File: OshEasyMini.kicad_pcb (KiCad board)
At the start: 6 copper layers, 20 x 37.4 mm, 119 parts, among them J1 TAGCONNECT, J10 Conn_01x04_MountingPin, J11 Conn_01x02, J3 SMA_Edgelaunch, J5 UFL, J6 Conn_01x05, J7 Conn_01x06, J8 Conn_01x02, Q1 SiA449DJ, Q2 AO3400A, Q3 SiA449DJ, U11 CPT-7502-65-SMT-TR, U12 LM293QT, U17 MCP73831-2-OT, U18 TC2185-3.3VxCTTR, U19 W25Q64JVXGIQ, U2 WE-TVS-82400102, U20 SISB46DN, U21 SN74LVC1G80QDCKTQ1, U3 ADXL375, U4 MS5607-02BA, U5 MAX-M10S, U6 MCP130-xxxxTT, U7 DRV5012AEDMRR, U8 CC1200, U9 ATSAMD21G17D-A, X2 ECS-160-8-36Q-AES-TR1, Y1 ABM8W-40.0000MHZ

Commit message: good progress, changed to mia-m10
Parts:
- removed C11, C12, C14, C15, C28: 47nF, Capacitor_SMD:C_0402_1005Metric
- removed J11: Conn_01x02, Connector_PinHeader_2.54mm:PinHeader_1x02_P2.54mm_Vertical_SMD_Pin1Left
- removed J6: Conn_01x05, Connector_PinHeader_2.54mm:PinHeader_1x05_P2.54mm_Vertical
- removed J7: Conn_01x06, Connector_PinHeader_2.54mm:PinHeader_1x06_P2.54mm_Vertical
- removed J8: Conn_01x02, Connector_PinHeader_2.54mm:PinHeader_1x02_P2.54mm_Vertical
- removed R38, R39: 1k, Resistor_SMD:R_0402_1005Metric
- removed U5: MAX-M10S, RF_GPS:ublox_MAX
- added C47: 47nF, Capacitor_SMD:C_0201_0603Metric, B.Cu at (95.7, 43.4)
- added C48: 47nF, Capacitor_SMD:C_0201_0603Metric, B.Cu at (94.7, 35.7)
- added C49: 47nF, Capacitor_SMD:C_0201_0603Metric, B.Cu at (99.8, 41.2)
- added C50: 47nF, Capacitor_SMD:C_0201_0603Metric, B.Cu at (95.0, 43.4)
- added C51: 47nF, Capacitor_SMD:C_0201_0603Metric, B.Cu at (97.2, 43.4)
- added C52: 47pF, Capacitor_SMD:C_0402_1005Metric, B.Cu at (97.0, 55.1)
- added FL1: SAFFB1G58KA0F0A, Filter:Filter_1109-5_1.1x0.9mm, B.Cu at (95.9, 55.3)
- added J2: Screw_Terminal_01x03, FCU2025Lib:Horizontal2.5mmWago3pin, F.Cu at (94.1, 55.0)
- added J4: Conn_01x02, Connector_JST:JST_PH_B2B-PH-K_1x02_P2.00mm_Vertical, F.Cu at (100.6, 62.1)
- added R55: 100k, Resistor_SMD:R_0201_0603Metric, F.Cu at (94.5, 58.6)
- added R57: 0, Resistor_SMD:R_0201_0603Metric, B.Cu at (97.5, 47.4)
- added R58: 0, Resistor_SMD:R_0201_0603Metric, B.Cu at (97.6, 46.8)
- added R59: 1k, Resistor_SMD:R_0201_0603Metric, F.Cu at (94.5, 60.3)
- added U1: MIA-M10Q, Package_LGA:ublox_LGA-53_4.5x4.5mm_Layout9x9_P0.5mm, B.Cu at (93.3, 51.4)
- added Y2: 32.768khz, Crystal:Crystal_SMD_2012-2Pin_2.0x1.2mm, B.Cu at (93.2, 55.7)
- C29, C30, C32, C34: footprint Capacitor_SMD:C_0402_1005Metric -> Capacitor_SMD:C_0201_0603Metric
- R11, R50, R51, R53, R56: footprint Resistor_SMD:R_0402_1005Metric -> Resistor_SMD:R_0201_0603Metric
- R52: value 100k -> 1k; footprint Resistor_SMD:R_0402_1005Metric -> Resistor_SMD:R_0201_0603Metric
- Y1: value ABM8W-40.0000MHZ -> 40mhz 8pF 30 Ohms; footprint Crystal:Crystal_SMD_Abracon_ABM8G-4Pin_3.2x2.5mm -> Crystal:Crystal_SMD_Abracon_ABM10-4Pin_2.5x2.0mm
- moved R9 79.9 mm to (130.4, 51.7), turned to -90 degrees
- moved R10 79.6 mm to (130.4, 49.8), turned to 90 degrees
- moved U2 74.6 mm to (127.8, 50.9), turned to 180 degrees
- moved C19 27.7 mm to (100.8, 46.5), turned to 0 degrees
- moved C16 26.8 mm to (104.0, 41.1), turned to -90 degrees
- moved C45 25.7 mm to (104.0, 39.3), turned to -90 degrees
- moved J10 24.9 mm to (134.2, 50.3)
- moved C5 20.2 mm to (92.0, 45.8), turned to 0 degrees
- moved U9 19.8 mm to (98.4, 40.8), turned to -90 degrees
- moved D3 17.7 mm to (126.4, 58.4)
- moved R4 17.7 mm to (125.9, 56.0)
- moved R3 17.7 mm to (126.9, 56.1)
- moved X2 17.0 mm to (91.7, 43.5), turned to -90 degrees
- moved U19 14.3 mm to (100.4, 50.4), turned to 90 degrees
- moved C6 14.2 mm to (91.7, 41.3), turned to 180 degrees
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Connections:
- C32 pad 2: Net-(U8-DCPL_PFD_CHP) -> +3V3
- C34 pad 2: Net-(U8-DCPL_XOSC) -> +3V3
- R51 pad 1: Net-(D5-A1) -> Net-(U21-D)
- R51 pad 2: Net-(U21-D) -> Net-(D5-A1)
- R52 pad 1: GND -> Net-(D4-K1)
- R52 pad 2: Net-(JP1-A) -> GND
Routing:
- net VBUS: track 2.33 -> 9.09 mm
- net /NRST: track 0.35 -> 5.91 mm, vias 0 -> 1
- net Net-(J10-Pin_1): track 0.00 -> 4.71 mm
- net Net-(J5-In): track 6.87 -> 3.14 mm
- net Net-(D6-A): track 0.00 -> 3.33 mm
- net Net-(U8-LPF0): track 0.00 -> 3.13 mm
- net Net-(U1-RF_IN): track 0.00 -> 2.77 mm
- net Net-(U1-RTC_O): track 0.00 -> 2.58 mm
- net Net-(U1-RTC_I): track 0.00 -> 2.48 mm
- net Net-(U8-DCPL_PFD_CHP): track 3.91 -> 1.72 mm
- net Net-(J10-Pin_2): track 0.00 -> 1.99 mm
- net Net-(U8-DCPL_XOSC): track 3.37 -> 1.56 mm
- net GND: track 16.4 -> 18.2 mm, vias 10 -> 4
- net Net-(U1-VCC_RF): track 1.90 -> 3.55 mm, vias 0 -> 2
- net +3V3: track 38.3 -> 39.9 mm, vias 8 -> 4
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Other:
- board size 20 x 37.4 mm -> 17.2 x 35.4 mm

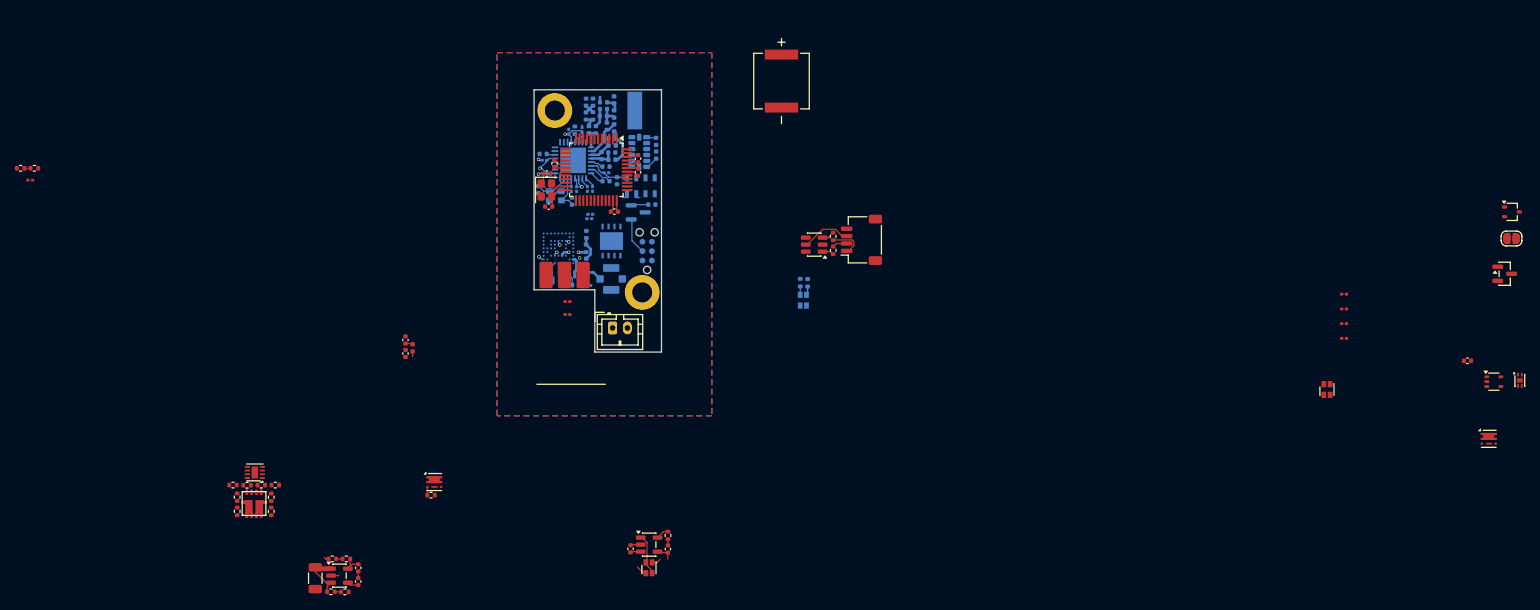
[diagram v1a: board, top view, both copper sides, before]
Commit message: all components placed currently routing
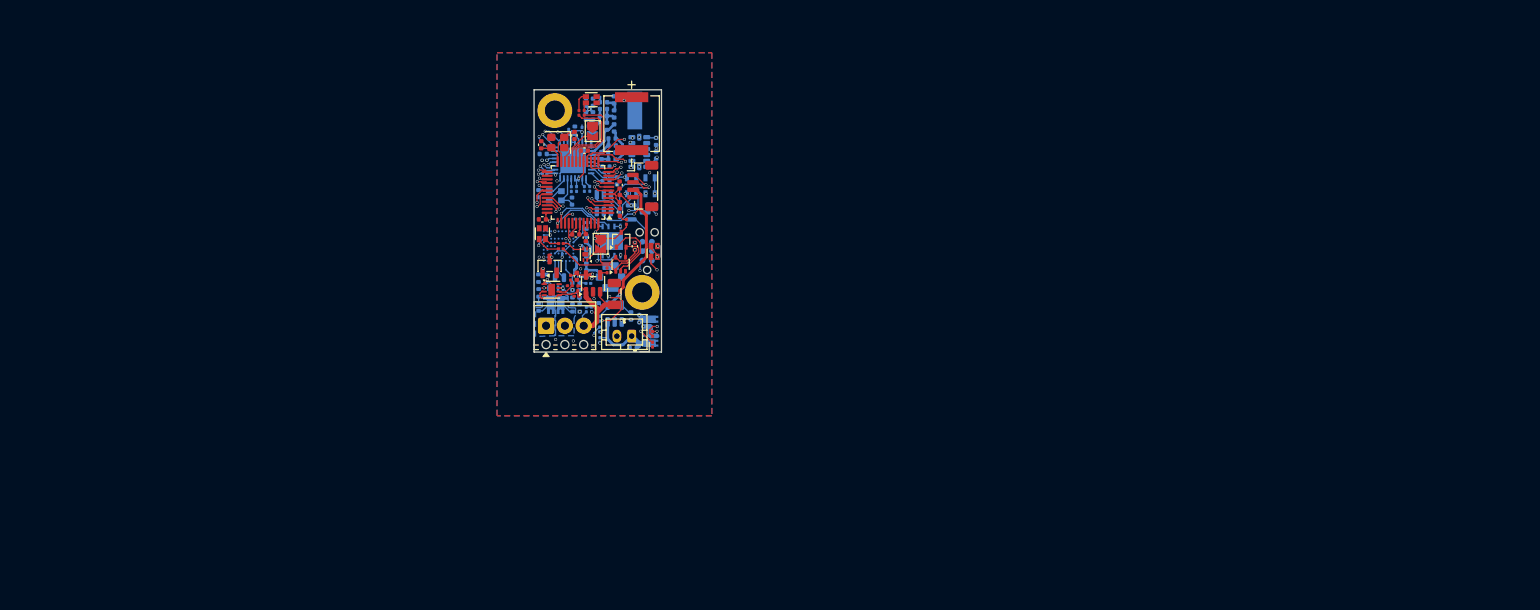
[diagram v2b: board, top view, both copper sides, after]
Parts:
- removed J2: Screw_Terminal_01x03, FCU2025Lib:Horizontal2.5mmWago3pin
- removed R10: 22, Resistor_SMD:R_0402_1005Metric
- removed R4: 1k, Resistor_SMD:R_0402_1005Metric
- added J6: Conn_01x02, Connector_JST:JST_PH_B2B-PH-K_1x02_P2.00mm_Vertical, F.Cu at (103.2, 63.2)
- added JP2: SolderJumper_2_Open, Jumper:SolderJumper-2_P1.3mm_Open_TrianglePad1.0x1.5mm, F.Cu at (97.9, 35.6)
- added R1: 22, Resistor_SMD:R_0201_0603Metric, B.Cu at (101.5, 45.5)
- added R2: 1k, Resistor_SMD:R_0201_0603Metric, F.Cu at (96.1, 33.1)
- C20, C21, Q1, Q3, R11, R13, R14, R15, R16, R17, R18, R19, R20, R37, R52, R59, U17, U2, U20: moved to B.Cu
- C22: footprint Capacitor_SMD:C_0402_1005Metric -> Capacitor_SMD:C_0201_0603Metric
- D3: moved to F.Cu
- J10: footprint Connector_JST:JST_SH_SM04B-SRSS-TB_1x04-1MP_P1.00mm_Horizontal -> Connector_JST:JST_SH_BM04B-SRSS-TB_1x04-1MP_P1.00mm_Vertical
- J4: value Conn_01x02 -> Screw_Terminal_01x03; footprint Connector_JST:JST_PH_B2B-PH-K_1x02_P2.00mm_Vertical -> TerminalBlock_Phoenix:TerminalBlock_Phoenix_MPT-0,5-3-2.54_1x03_P2.54mm_Horizontal
- JP1: footprint Jumper:SolderJumper-2_P1.3mm_Open_RoundedPad1.0x1.5mm -> Jumper:SolderJumper-2_P1.3mm_Open_TrianglePad1.0x1.5mm
- R3: footprint Resistor_SMD:R_0402_1005Metric -> Resistor_SMD:R_0201_0603Metric; moved to F.Cu
- R40, R41, R42, R43, R49: footprint Resistor_SMD:R_0402_1005Metric -> Resistor_SMD:R_0201_0603Metric
- R46, R47, R9: footprint Resistor_SMD:R_0402_1005Metric -> Resistor_SMD:R_0201_0603Metric; moved to B.Cu
- Y2: footprint Crystal:Crystal_SMD_2012-2Pin_2.0x1.2mm -> Crystal:Crystal_SMD_MicroCrystal_CM9V-T1A-2Pin_1.6x1.0mm
- moved Q2 128.9 mm to (92.1, 53.8), turned to 90 degrees
- moved U7 127.3 mm to (96.9, 52.2), turned to 180 degrees
- moved JP1 123.0 mm to (99.0, 50.8), turned to -90 degrees
- moved D2 120.3 mm to (101.8, 50.2), turned to 90 degrees
- moved U21 118.9 mm to (101.7, 53.6), turned to 90 degrees
- moved Q3 114.3 mm to (105.7, 61.3), turned to 180 degrees
- moved C44 113.4 mm to (103.6, 51.1), turned to -90 degrees
- moved D5 107.9 mm to (91.2, 49.4), turned to 180 degrees
- moved R51 106.0 mm to (93.6, 51.5), turned to 180 degrees
- moved R50 105.9 mm to (93.6, 50.7)
- moved R52 100.5 mm to (98.8, 62.4), turned to -90 degrees
- moved R53 93.3 mm to (106.0, 62.9), turned to 90 degrees
- moved R11 79.8 mm to (98.9, 63.8), turned to 90 degrees
- moved R47 79.4 mm to (97.8, 59.6), turned to 90 degrees
- moved R46 76.9 mm to (97.1, 59.7), turned to -90 degrees
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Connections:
- D5 pad 2: Net-(D5-A1) -> Net-(D5-A2)
- J4 pad 1: V_CHARGE -> /FET_B
- J4 pad 2: GND -> /FET_A
- Q1 pad 4: /V_PROT -> /MGSW_IN
- R51 pad 2: Net-(D5-A1) -> Net-(D5-A2)
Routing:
- net /MGSW_IN: track 0.00 -> 30.1 mm, vias 0 -> 3
- net Net-(Q2-D): track 0.00 -> 28.5 mm, vias 0 -> 2
- net /CS_RADIO: track 0.44 -> 26.4 mm, vias 0 -> 2
- net VBUS: track 9.09 -> 29.6 mm, vias 0 -> 2
- net /MOSI3: track 0.59 -> 20.4 mm, vias 0 -> 2
- net /BUZZ: track 0.00 -> 19.4 mm, vias 0 -> 2
- net /AC_INT2: track 0.00 -> 19.3 mm, vias 0 -> 2
- net /AC_INT1: track 0.00 -> 18.1 mm, vias 0 -> 2
- net Net-(D4-K1): track 1.50 -> 18.2 mm, vias 0 -> 2
- net Net-(U21-D): track 0.00 -> 16.5 mm
- net Net-(D4-A2): track 1.27 -> 16.4 mm, vias 0 -> 3
- net Net-(JP1-A): track 0.00 -> 14.6 mm, vias 0 -> 2
- net /CS_FLASH: track 0.00 -> 13.3 mm, vias 0 -> 2
- net /RADIO_MARC_ISR: track 0.34 -> 13.0 mm, vias 0 -> 2
- net /TX1: track 0.00 -> 12.7 mm, vias 0 -> 2
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- added copper zone on B.Cu, net /FET_A
- added copper zone on B.Cu, net /FET_B
- added copper zone on In2.Cu, net V_LIPO
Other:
- outline, holes or cut-outs redrawn

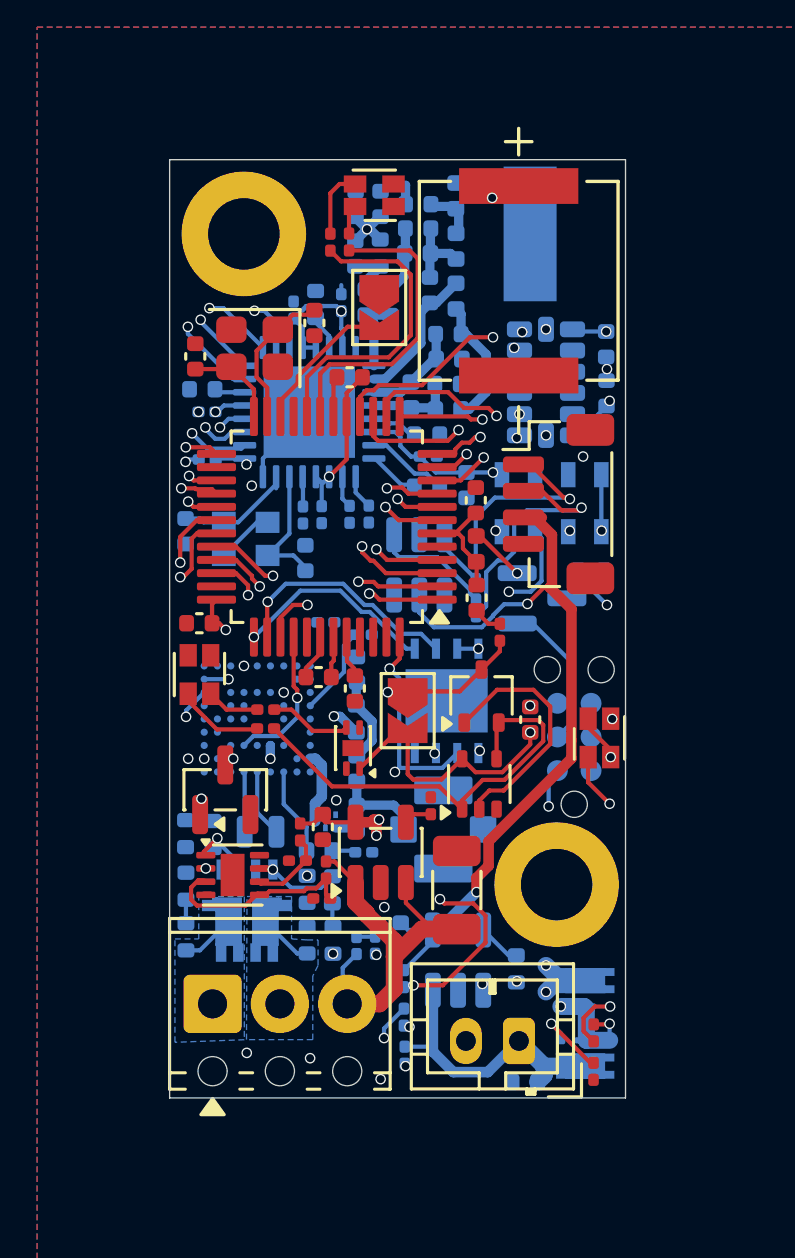
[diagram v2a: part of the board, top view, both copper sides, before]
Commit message: routing done, need to remove SAW and impedance match
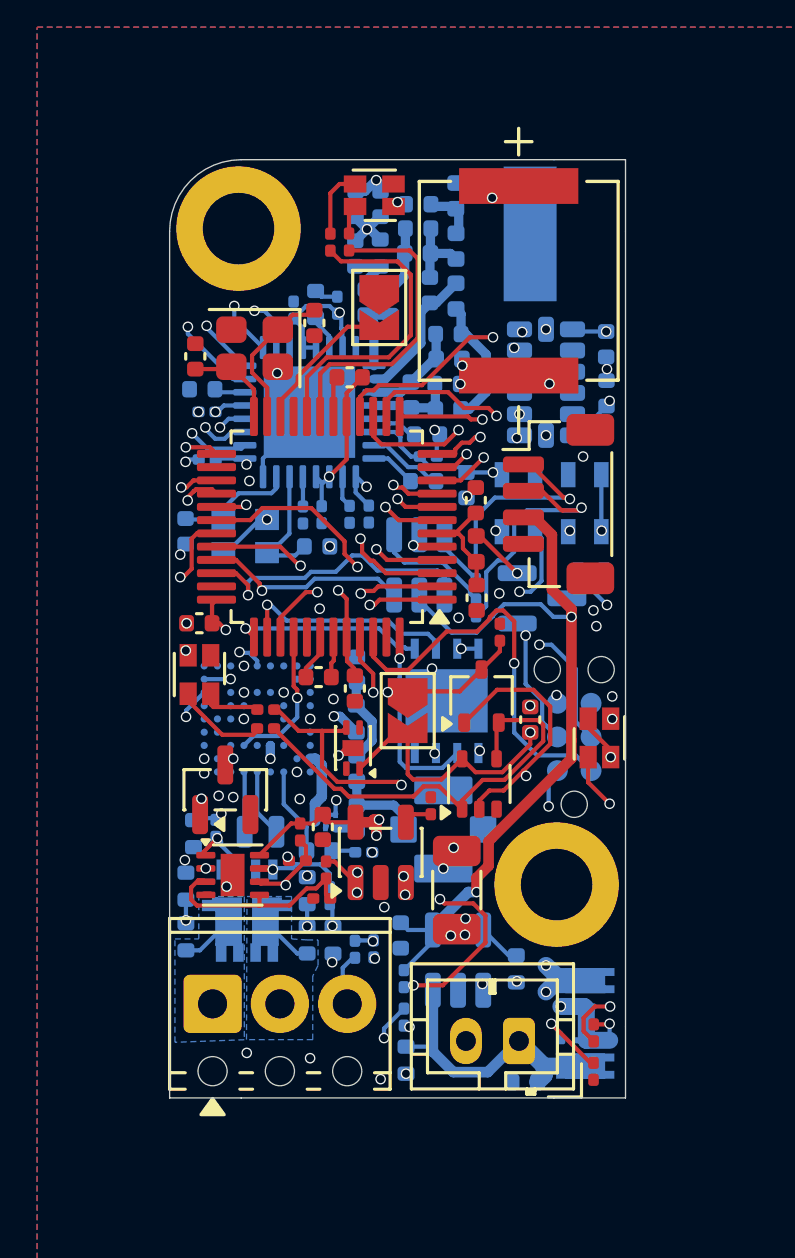
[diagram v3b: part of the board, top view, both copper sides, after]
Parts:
- removed R11: 56k, Resistor_SMD:R_0201_0603Metric
- removed R17, R20: 1k, Resistor_SMD:R_0402_1005Metric
- removed R57, R58: 0, Resistor_SMD:R_0201_0603Metric
- added R21: 56k, Resistor_SMD:R_0402_1005Metric, B.Cu at (98.9, 64.0)
- added R4: 1k, Resistor_SMD:R_0201_0603Metric, B.Cu at (96.0, 57.8)
- added R5: 1k, Resistor_SMD:R_0201_0603Metric, B.Cu at (91.7, 55.2)
- R15, R16: value 12k -> 27k
- R46: value 100k -> 5.6k
- R47: value 27k -> 10k
- moved C26 0.62 mm to (95.6, 44.6), turned to 180 degrees
- moved R19 0.30 mm to (90.9, 55.4)
- moved H2 0.28 mm to (92.6, 32.6)
- moved C27 0.25 mm to (99.6, 42.1)
- moved C29 0.18 mm to (96.3, 35.5)
- moved R46 0.15 mm to (97.0, 59.8)
- moved R47 0.15 mm to (97.7, 59.8)
- moved Y1 0.11 mm to (92.8, 44.2)
- moved R15 0.05 mm to (95.2, 57.6)
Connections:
- U1 pad F9: Net-(R57-Pad1) -> GND
- U1 pad G7: Net-(R58-Pad1) -> GND
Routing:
- net Net-(U1-V_BCKP): track 0.11 -> 38.1 mm, vias 1 -> 4
- net /SENSE_B: track 7.58 -> 40.8 mm, vias 1 -> 2
- net /NRST: track 13.9 -> 44.6 mm, vias 2 -> 3
- net /SENSE_A: track 4.20 -> 29.8 mm, vias 1 -> 2
- net /V_BATT: track 5.97 -> 28.1 mm, vias 1 -> 2
- net /FIRE_A: track 2.30 -> 22.7 mm, vias 1 -> 2
- net /MISO3: track 1.23 -> 20.7 mm
- net /SWCLK: track 0.00 -> 17.8 mm, vias 0 -> 2
- net /CS_BARO: track 4.88 -> 20.6 mm
- net /SWDIO: track 0.00 -> 15.1 mm, vias 0 -> 1
- net /FIRE_B: track 2.08 -> 17.0 mm, vias 1 -> 2
- net /MISO5: track 10.7 -> 25.3 mm, vias 3 -> 2
- net /MOSI5: track 10.8 -> 22.6 mm
- net /SCK5: track 11.4 -> 22.5 mm
- net V_LIPO: track 16.8 -> 6.08 mm, vias 2 -> 9
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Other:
- outline, holes or cut-outs redrawn

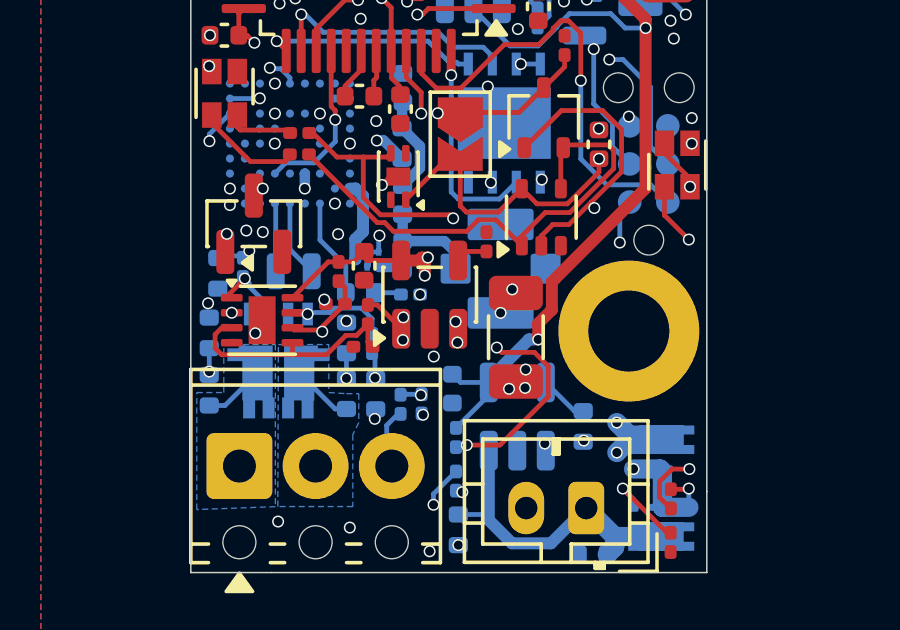
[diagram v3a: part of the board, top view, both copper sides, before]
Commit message: finished usbc daughterboard, next removing charging circuitry onboard
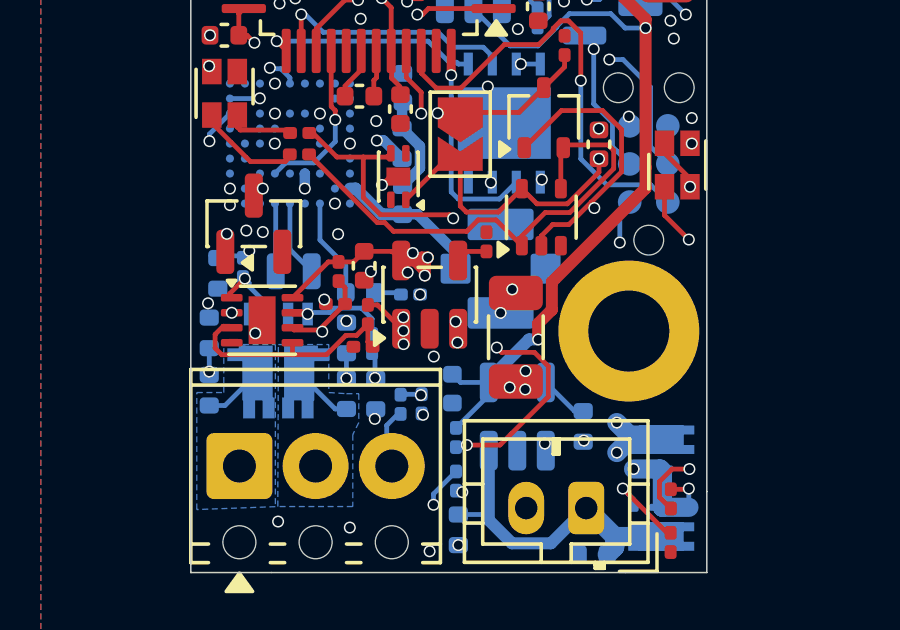
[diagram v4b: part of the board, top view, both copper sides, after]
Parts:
- removed C52: 47pF, Capacitor_SMD:C_0402_1005Metric
- removed FL1: SAFFB1G58KA0F0A, Filter:Filter_1109-5_1.1x0.9mm
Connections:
- U1 pad B9: Net-(U1-RF_IN) -> Net-(J5-In)
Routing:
- net Net-(U1-RF_IN): track 2.77 -> 0.00 mm
- net Net-(J5-In): track 3.67 -> 5.25 mm
- net +3V3: track 45.5 -> 47.1 mm, vias 20 -> 22
- net GND: track 16.7 -> 15.2 mm
- net Net-(C52-Pad2): track 0.84 -> 0.00 mm
- net V_LIPO: vias 9 -> 10
